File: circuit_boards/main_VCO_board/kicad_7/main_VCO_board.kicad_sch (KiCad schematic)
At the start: 17 parts, among them J1 VCF_BOARD_CON, J2 MOD_BOARD_CON, J3 VCO_EXT_CON, SW11 E-Switch_EG2301, SW12 E-Switch_EG2301, SW13 E-Switch_EG2301, SW5 E-Switch_EG2301, SW9 E-Switch_EG2301, U1 TL072

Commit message: Progress on circuit boards
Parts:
- RV503: footprint Potentiometer_THT:Potentiometer_Alpha_RD901F-40-00D_Single_Vertical -> custom_footprints:Bourns_PTV09
- SW11, SW12, SW5, SW9: value E-Switch_EG2301 -> E-Switch_EG2301B
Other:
- note removed: "TODO scale RM inputs"
- moved on the sheet: RV503, SW11A, SW11B, SW12B

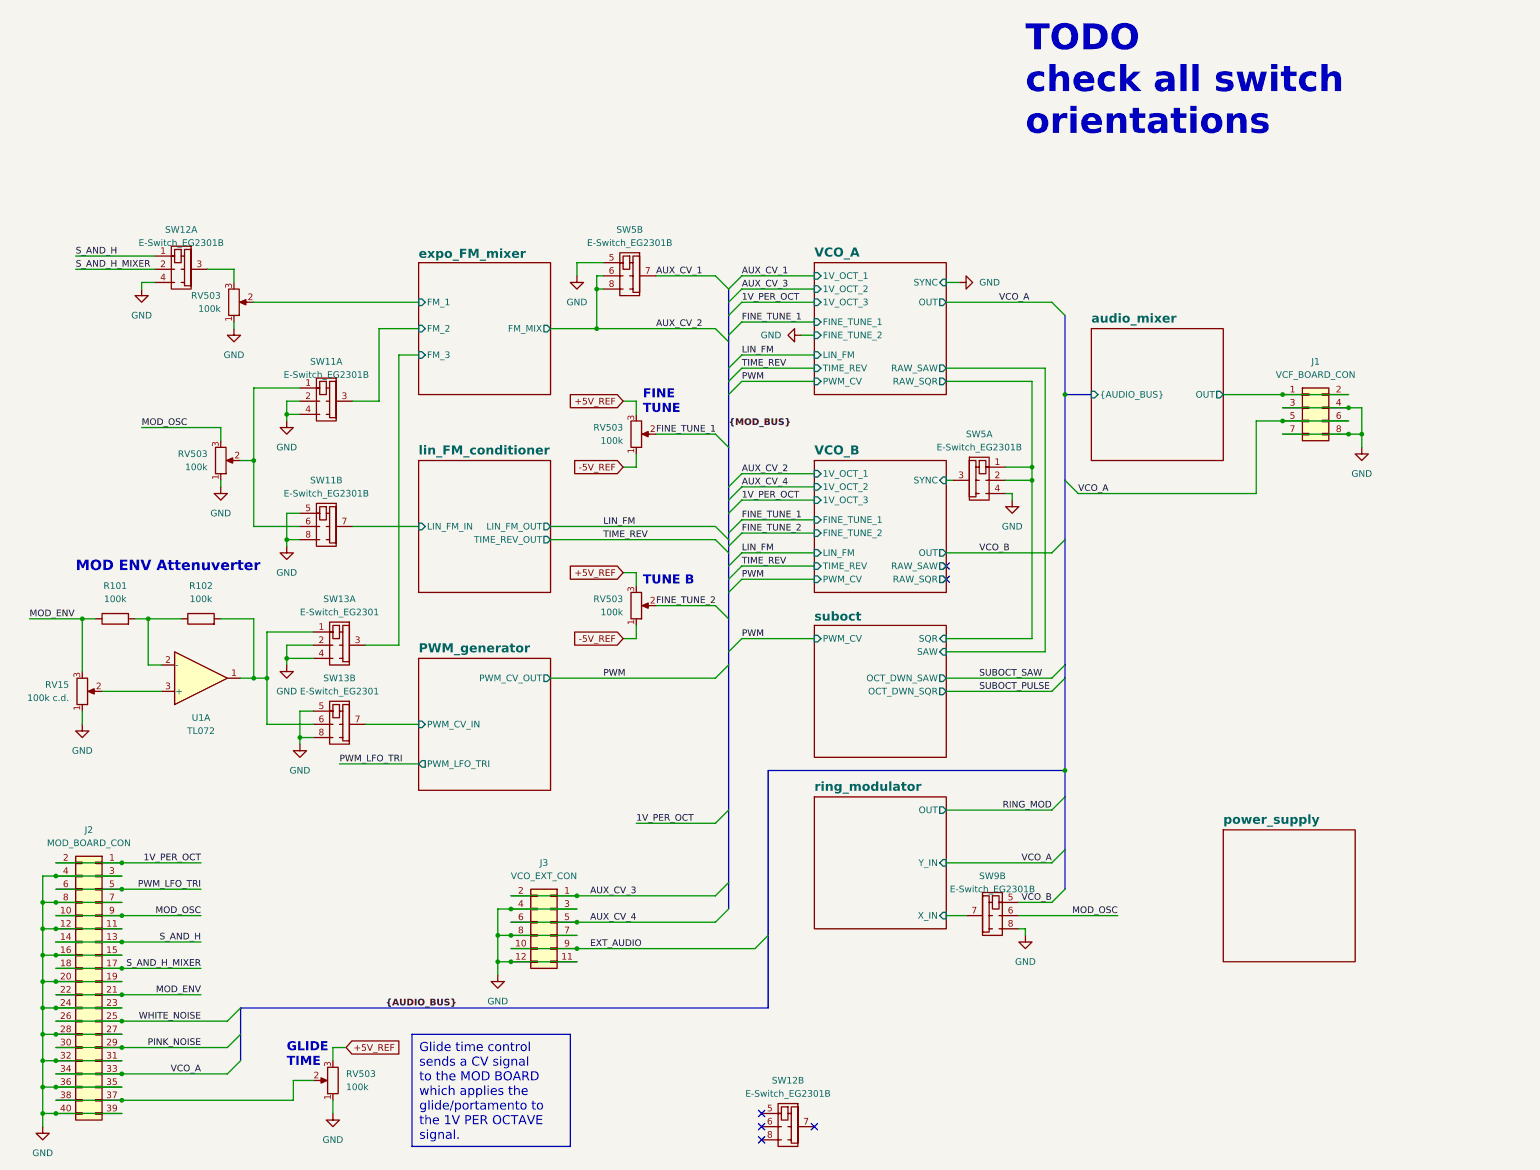
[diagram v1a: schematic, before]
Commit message: Update PCBs, tweak vals, add VCF CV from DAC
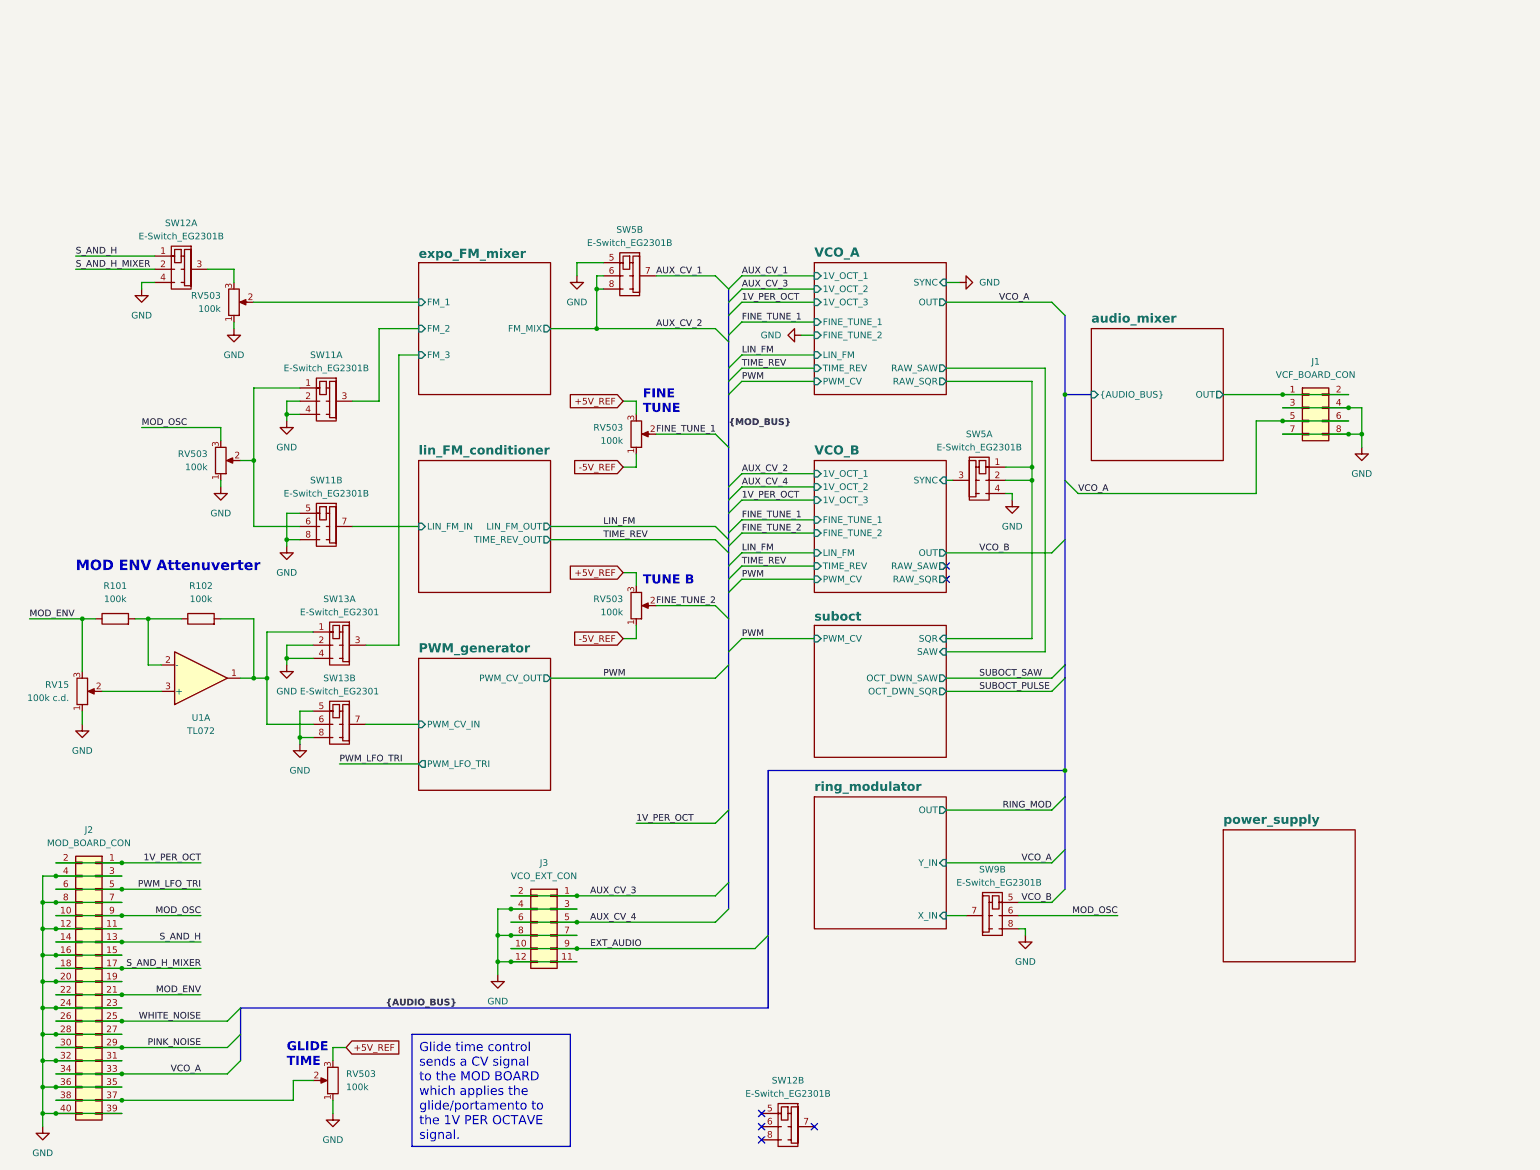
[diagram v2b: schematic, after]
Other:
- note removed: "TODO check all switch orientations"
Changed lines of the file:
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@@
     (comment 4 "Author: Jordan Aceto")
   )
+  (bus_alias "MOD_BUS" (members "1V_PER_OCT" "LIN_FM" "TIME_REV" "PWM" "AUX_CV_1" "AUX_CV_2" "AUX_CV_3" "AUX_CV_4" "FINE_TUNE_1" "FINE_TUNE_2"))
   (bus_alias "AUDIO_BUS" (members "VCO_A" "VCO_B" "SUBOCT_SAW" "RING_MOD" "WHITE_NOISE" "EXT_AUDIO" "SUBOCT_PULSE" "PINK_NOISE" ""))
-  (bus_alias "MOD_BUS" (members "1V_PER_OCT" "LIN_FM" "TIME_REV" "PWM" "AUX_CV_1" "AUX_CV_2" "AUX_CV_3" "AUX_CV_4" "FINE_TUNE_1" "FINE_TUNE_2"))
   (junction (at 262.89 55.88) (diameter 0) (color 0 0 0 0)
   )
@@
     (effects (font (size 1.75 1.75) (thickness 0.35) bold) (justify left bottom))
   )
-  (text "TODO\ncheck all switch \norientations" (at 213.36 1.27 0)
-    (effects (font (size 5 5) (thickness 0.6) bold) (justify left bottom))
-  )
   (label "{MOD_BUS}" (at 156.21 57.15 0) (fields_autoplaced)
     (effects (font (size 1.27 1.27) bold) (justify left bottom))
@@
   )
   (symbol (lib_id "custom_symbols:E-Switch_EG2301") (at 50.8 26.67 0) (mirror y) (unit 1)
-    (in_bom yes) (on_board yes) (dnp no) (fields_autoplaced)
-    (property "Reference" "SW12" (at 50.8 19.05 0)
-      (effects (font (size 1.27 1.27)))
-    )
-    (property "Value" "E-Switch_EG2301B" (at 50.8 21.59 0)
+    (in_bom yes) (on_board yes) (dnp no)
+    (property "Reference" "SW12" (at 50.8 17.78 0)
+      (effects (font (size 1.27 1.27)))
+    )
+    (property "Value" "E-Switch_EG2301B" (at 50.8 20.32 0)
       (effects (font (size 1.27 1.27)))
     )
@@
   )
   (symbol (lib_id "custom_symbols:E-Switch_EG2301") (at 78.74 52.07 0) (mirror y) (unit 1)
-    (in_bom yes) (on_board yes) (dnp no) (fields_autoplaced)
-    (property "Reference" "SW11" (at 78.74 44.45 0)
-      (effects (font (size 1.27 1.27)))
-    )
-    (property "Value" "E-Switch_EG2301B" (at 78.74 46.99 0)
+    (in_bom yes) (on_board yes) (dnp no)
+    (property "Reference" "SW11" (at 78.74 43.18 0)
+      (effects (font (size 1.27 1.27)))
+    )
+    (property "Value" "E-Switch_EG2301B" (at 78.74 45.72 0)
       (effects (font (size 1.27 1.27)))
     )
@@
   )
   (symbol (lib_id "custom_symbols:E-Switch_EG2301") (at 207.01 151.13 0) (unit 2)
-    (in_bom yes) (on_board yes) (dnp no) (fields_autoplaced)
-    (property "Reference" "SW9" (at 207.01 143.51 0)
-      (effects (font (size 1.27 1.27)))
-    )
-    (property "Value" "E-Switch_EG2301B" (at 207.01 146.05 0)
-      (effects (font (size 1.27 1.27)))
-    )
+    (in_bom yes) (on_board yes) (dnp no)
+    (property "Reference" "SW9" (at 207.01 142.24 0)
+      (effects (font (size 1.27 1.27)))
+    )
+    (property "Value" "E-Switch_EG2301B" (at 208.28 144.78 0)
+      (effects (font (size 1.27 1.27)))
+    )

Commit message: Add potentiometer 3d model to VCO and MOD boards
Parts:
- RV15, RV503: footprint Potentiometer_THT:Potentiometer_Alpha_RD901F-40-00D_Single_Vertical -> custom_footprints:Potentiometer_Alpha_RD901F-40-00D_Single_Vertical
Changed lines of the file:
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@@
     (comment 4 "Author: Jordan Aceto")
   )
+  (bus_alias "MOD_BUS" (members "1V_PER_OCT" "LIN_FM" "TIME_REV" "PWM" "AUX_CV_1" "AUX_CV_2" "AUX_CV_3" "AUX_CV_4" "FINE_TUNE_1" "FINE_TUNE_2"))
   (bus_alias "AUDIO_BUS" (members "VCO_A" "VCO_B" "SUBOCT_SAW" "RING_MOD" "WHITE_NOISE" "EXT_AUDIO" "SUBOCT_PULSE" "PINK_NOISE" ""))
-  (bus_alias "MOD_BUS" (members "1V_PER_OCT" "LIN_FM" "TIME_REV" "PWM" "AUX_CV_1" "AUX_CV_2" "AUX_CV_3" "AUX_CV_4" "FINE_TUNE_1" "FINE_TUNE_2"))
   (junction (at 262.89 55.88) (diameter 0) (color 0 0 0 0)
   )
@@
       (effects (font (size 1.27 1.27)) (justify right))
     )
-    (property "Footprint" "Potentiometer_THT:Potentiometer_Alpha_RD901F-40-00D_Single_Vertical" (at 60.96 33.02 0)
+    (property "Footprint" "custom_footprints:Potentiometer_Alpha_RD901F-40-00D_Single_Vertical" (at 60.96 33.02 0)
       (effects (font (size 1.27 1.27)) hide)
     )
@@
       (effects (font (size 1.27 1.27)) (justify right))
     )
-    (property "Footprint" "Potentiometer_THT:Potentiometer_Alpha_RD901F-40-00D_Single_Vertical" (at 138.43 91.44 0)
+    (property "Footprint" "custom_footprints:Potentiometer_Alpha_RD901F-40-00D_Single_Vertical" (at 138.43 91.44 0)
       (effects (font (size 1.27 1.27)) hide)
     )
@@
       (effects (font (size 1.27 1.27)) (justify right))
     )
-    (property "Footprint" "Potentiometer_THT:Potentiometer_Alpha_RD901F-40-00D_Single_Vertical" (at 31.75 107.95 0)
+    (property "Footprint" "custom_footprints:Potentiometer_Alpha_RD901F-40-00D_Single_Vertical" (at 31.75 107.95 0)
       (effects (font (size 1.27 1.27)) hide)
     )
@@
       (effects (font (size 1.27 1.27)) (justify right))
     )
-    (property "Footprint" "Potentiometer_THT:Potentiometer_Alpha_RD901F-40-00D_Single_Vertical" (at 58.42 63.5 0)
+    (property "Footprint" "custom_footprints:Potentiometer_Alpha_RD901F-40-00D_Single_Vertical" (at 58.42 63.5 0)
       (effects (font (size 1.27 1.27)) hide)
     )
@@
       (effects (font (size 1.27 1.27)) (justify right))
     )
-    (property "Footprint" "Potentiometer_THT:Potentiometer_Alpha_RD901F-40-00D_Single_Vertical" (at 138.43 58.42 0)
-      (effects (font (size 1.27 1.27)) hide)
-    )
+    (property "Footprint" "custom_footprints:Potentiometer_Alpha_RD901F-40-00D_Single_Vertical" (at 138.43 58.42 0)
+      (effects (font (size 1.27 1.27)) hide)
+    )
